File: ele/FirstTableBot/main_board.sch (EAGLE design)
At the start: 118 parts, among them IC3 CP2102N-28, T1 BC337, T2 BC337, U1 ESP-WROOM-32, X3 USB-MICRO-B-BOTTOM, X4 POWER_IN

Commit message: ir led pro encodery
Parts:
- removed !CTS, !DCD, !DSR, !DTR, !RESET, !RTS, !SUSPEND, CHR0, CHR1, CHREN, IO0/TXLED, IO1/RXLED, IO2/RS485, IO3/WAKEUP, IO4, IO5, IO6, RI/CLK, RXD, SUSPEND, TXD: PINH1X01, pinhead_smd:PINH1X01
- removed C10, C14: 100n/16V, rcl_upravena:C-EUC0402
- removed C11, C18: 4u7/16V, rcl_upravena:C-EUC0603
- removed IC3: CP2102N-28, CP2102N:CP2102N-28
- removed IM1: STEPDOWN, StepDown:STEPDOWN
- removed JP1: PINH2X06, pinhead_smd:PINH2X06
- removed LED6, LED7, LED8: yellow, led:LEDCHIP-LED0603
- removed LED_3V3: green, led:LEDCHIPLED_0603
- removed NC2: NC, NC:NC
- removed R29, R30: 180R, rcl_upravena:R-EU_R0603
- removed R31: 470R, rcl_upravena:R-EU_R0603
- removed R58: 10k, rcl_upravena:R-EU_R0603
- removed RN1: (no value), resistor-dil:2R-NEXB24V
- removed T1, T2: BC337, transistors:NPN-SOT23-BEC
- removed U1: ESP-WROOM-32, esp32:ESP-WROOM-32
- removed USB: (no value), pinhead:PINHD-1X5
- removed X3: USB-MICRO-B-BOTTOM, usb:USB-MICRO-B-BOTTOM
- added D2: (no value), diode:DIODE-D-7.5
- added IM6: DEVKITC, esp32:DEVKITC
- added JP2: (no value), pinhead:PINHD-1X6
- added R32, R33, R34, R35: (no value), resistor:R-EU_R0603
- added U$10, U$12, U$13, U$14: L-NP-3C1, led-brt:L-NP-3C1
- added U$16, U$17, U$18, U$19: BIR-NM13C1, led-brt:BIR-NM13C1
- LED0, LED1, LED2, LED3, LED4: device led:LED3MM -> led:LEDCHIPLED_1206
- LED5: value BLUE -> GREEN
- Q2, Q5: device transistors:P-MOSFET-TO220V -> transistors:P-MOSFET-MLP_HS
- R19, R62: device resistor:R-EU_M1206 -> resistor:R-EU_R0603
- R23: value 470R -> (none); device rcl_upravena:R-EU_R0603 -> resistor:R-EU_R0805
- R25, R26: value 470R -> (none); device rcl_upravena:R-EU_R0603 -> resistor:R-EU_R0603
- R27, R28: value 10k -> (none); device rcl_upravena:R-EU_R0603 -> resistor:R-EU_R0603
- RN2: device resistor-dil:4R-N0402ARV341 -> resistor-dil:4R-NEXBS8V
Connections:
- removed net !DTR: !DTR.1, IC3.!DTR, R27.1, T2.E
- removed net !DTR_B: R27.2, T1.B
- removed net !RESET: !RESET.1, IC3.!RESET, R58.1
- removed net !RTS: !RTS.1, IC3.!RTS, R28.1, T1.E
- removed net !RTS_B: R28.2, T2.B
- removed net !SUSPEND: !SUSPEND.1, IC3.!SUSPEND
- removed net CHR0: CHR0.1, IC3.CHR0
- removed net CHR1: CHR1.1, IC3.CHR1
- removed net CHREN: CHREN.1, IC3.CHREN
- removed net CLK/!RI: IC3.CLK/!RI, RI/CLK.1
- removed net DCD: !DCD.1, IC3.!DCD
- removed net DM: IC3.USBDM, USB.2, X3.D-
- removed net DP: IC3.USBDP, USB.3, X3.D+
- removed net DSR: !DSR.1, IC3.!DSR
- removed net EN: T1.C, U1.EN
- removed net IO0_!RST!_: T2.C, U1.IO0
- removed net IO12_: U1.IO12
- removed net IO13_: U1.IO13
- removed net IO14_: U1.IO14
- removed net IO15_: U1.IO15
- removed net IO16_: U1.IO16
- removed net IO17_: U1.IO17
- removed net IO18_: U1.IO18
- removed net IO19_: U1.IO19
- removed net IO21_: U1.IO21
- removed net IO22_: U1.IO22
- removed net IO23_: U1.IO23
- removed net IO25_: U1.IO25
- removed net IO26_: U1.IO26
- removed net IO27_: U1.IO27
- removed net IO2_: U1.IO2
- removed net IO32_: U1.IO32
- removed net IO33_: U1.IO33
- removed net IO34_: U1.IO34
- removed net IO35_: U1.IO35
- removed net IO4_: U1.IO4
- removed net IO5_: U1.IO5
- removed net IO9_NC1: IM1.EN, NC2.NC
- removed net LED_3V3: LED_3V3.C, R31.2
- removed net N$24: U$8.PB2/GPIO/CLK
- removed net NC-CS: U1.CMD
- removed net NC-HOLD: U1.SD2
- removed net NC-MISO: U1.SD1
- removed net NC-MOSI: U1.SD0
- removed net NC-SCK: U1.CLK
- removed net NC-WP: U1.SD3
- removed net PWM_A2: U$9.AIN2
- removed net PWM_B2: U$9.BIN2
- removed net RX-LED: LED7.C, R25.1
- removed net RXD: IC3.RXD, R30.1, RXD.1
- removed net RXD0_: R29.2, U1.RXD0
- removed net RX_LED: IC3.RXLED/IO1, IO1/RXLED.1, R25.2
- removed net SENSOR_VN_: U1.SENSOR_VN
- removed net SENSOR_VP_: U1.SENSOR_VP
- removed net SUSPEND: IC3.SUSPEND, R26.1, SUSPEND.1
- removed net TX-LED: LED6.C, R23.1
- removed net TXD: IC3.TXD, R29.1, TXD.1
- removed net TXD0_: R30.2, U1.TXD0
- removed net TX_LED: IC3.TXLED/IO0, IO0/TXLED.1, R23.2
- removed net USBID: USB.4, X3.ID
- removed net USBIO3_RS485: IC3.RS485/IO2, IO2/RS485.1
- removed net USBIO3_WAKEUP: IC3.WAKEUP/IO3, IO3/WAKEUP.1
- removed net USBIO4: IC3.IO4, IO4.1
- removed net USBIO5: IC3.IO5, IO5.1
- removed net USBIO6: IC3.IO6, IO6.1
- removed net VCCIO: C10.1, C18.1, IC3.VCC, LED6.A, LED7.A, LED8.A, R58.2
- removed net VUSB: C11.1, C14.1, IC3.VBUS, IC3.VREGIN, USB.1, X3.VBUS
- new net +5V_ESP: D2.C, IM6.5V
- new net CDA: IM6.IO2, U$8.PB2/GPIO/CLK
- new net ENC-A0: IM6.SVP, R32.2, U$10.PIN
- new net ENC-A1: IM6.SVN, R33.2, U$12.PIN
- new net ENC-B0: IM6.IO34, R34.2, U$13.PIN
- new net ENC-B1: IM6.IO35, R35.2, U$14.PIN
- new net N$18: R26.2, U$17.VCC
- new net N$19: R27.2, U$18.VCC
- new net N$20: R28.2, U$19.VCC
- new net PWM_A0: IM6.IO12, U$9.AIN1
- new net PWM_B0: IM6.IO17, U$9.BIN1
- net +3V3: now also IM6.3V3; no longer IM1.OUT, LED_3V3.A, U1.3V3
- net +5V: now also D2.A, JP2.2, R25.1, R26.1, R27.1, R28.1, R32.1, R33.1, R34.1, R35.1; no longer JP1B2.1, JP1T2.1
- net GND: now also IM6.GND, JP2.3, U$10.GND, U$12.GND, U$13.GND, U$14.GND, U$16.GND, U$17.GND, U$18.GND, U$19.GND; no longer C1.2, C10.2, C11.2, C14.2, C18.2, IC3.GND, IM1.GND, JP1B3.1, JP1T3.1, R18.2, R31.1, SW4.P, SW4.P1, U1.GND@1, U1.GND@2, U1.GND@3, U1.GND@4, USB.5, X3.GND
- net MISO: now also JP2.5; no longer JP1B5.1, JP1T5.1
- net MOSI: now also JP2.6; no longer JP1B6.1, JP1T6.1
- net N$12: now also R25.2, U$16.VCC; no longer !CTS.1, IC3.!CTS
- net N$13: now also C1.2, R18.2, SW4.P, SW4.P1; no longer LED8.C, R26.2
- net PB3: now also R23.1; no longer RN1A.1
- net PWM_A1: now also IM6.IO16, U$9.AIN2; no longer U$9.AIN1
- net PWM_B1: now also IM6.IO5, U$9.BIN2; no longer U$9.BIN1
- net RESET: now also JP2.1; no longer JP1B1.1, JP1T1.1
- net SCK: now also IM6.IO0, JP2.4; no longer JP1B4.1, JP1T4.1
- net SW4: now also R23.2; no longer RN1A.2
- net VCC: no longer IM1.IN
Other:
- note removed: "RobotikaBrno"
- note removed: "github:roboticsbrno/ RB3200-ESP32universal RobotikaBrno.cz Robotarna CC BY-SA 4.0"
- note removed: "v2.0"

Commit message: upravi elektra
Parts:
- removed JP2: (no value), pinhead:PINHD-1X6
- removed LED0: BLUE, led:LEDCHIPLED_1206
- removed RN2: (no value), resistor-dil:4R-NEXBS8V
- removed U$11: BA10358F-E2SOIC, Rohm:BA10358F-E2SOIC
- added JP1: (no value), pinhead:PINHD-1X3
- added R29, R39, R42, R45, R48: (no value), resistor:R-EU_R0805
- added R30, R31, R50, R51, R52, R53: (no value), resistor:R-EU_R0603
- added R38, R41, R44, R47: 620, resistor:R-EU_R0805
- added R40, R43, R46, R49: 10k, resistor:R-EU_R0805
- added U$15: MCP6022-E/ST, MCP6022-E_ST:MCP6022-E/ST
- LED4: value RED -> BLUE
- LED5: value GREEN -> BLUE; device led:LED3MM -> led:LEDCHIPLED_1206
- R19, R62: value (none) -> 22m
- R21, R22: value 5k -> 10k
- R23: value (none) -> 10k
- R24: value (none) -> 620; device resistor:R-EU_R0603 -> resistor:R-EU_R0805
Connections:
- removed net MISO: JP2.5, U$8.PA2/ADC/GPIO/MISO
- removed net MOSI: JP2.6, U$8.PA1/ADC/GPIO/MOSI
- removed net SW1: C3.2, JP4.8, LED2.A, RN2B.2, SW1.P, SW1.P1
- new net IR-LED-POWER: R1.1, R11.1, R13.1, R3.1, R5.1, R7.1, R9.1, U$8.PB2/CLK
- new net N$24: LED2.A, R41.2
- new net N$26: LED1.A, R38.2
- new net N$27: LED4.A, R44.2
- new net N$28: LED5.A, R47.2
- new net N$29: R51.2, R53.1, U$15.VINA-
- new net N$30: R50.2, R52.1, U$15.VINB-
- new net PC7: R47.1, R48.1, R49.1
- new net SW5: C3.2, JP4.8, R39.2, SW1.P, SW1.P1
- net +3V3: now also R30.1, R31.1
- net +5V: now also JP1.2, R23.2, R40.2, R43.2, R46.2, R49.2; no longer JP2.2, R1.1, R11.1, R13.1, R3.1, R5.1, R7.1, R9.1
- net ADC0: now also U$8.PA4/ADC; no longer U$8.PA4/ADC/GPIO
- net ADC1: now also U$8.PA5/ADC; no longer U$8.PA5/ADC/GPIO
- net ADC2: now also U$8.PA6/ADC; no longer U$8.PA6/ADC/GPIO
- net ADC3: now also U$8.PA7/ADC; no longer U$8.PA7/ADC/GPIO
- net ADC4: now also U$8.PB5/ADC; no longer U$8.PB5/ADC/GPIO
- net ADC5: now also U$8.PB4/ADC; no longer U$8.PB4/ADC/GPIO
- net ADC6: now also U$8.PB1/ADC; no longer U$8.PB1/ADC/GPIO
- net ADC7: now also U$8.PB0/ADC; no longer U$8.PB0/ADC/GPIO
- net AMPLIFIED_I-MOT_A: now also R53.2, U$15.VOUTA; no longer U$11.OUT2
- net AMPLIFIED_I-MOT_B: now also R52.2, U$15.VOUTB; no longer U$11.OUT1
- net BAT_POL+: no longer R24.2
- net CDA: now also IM6.IO22, R30.2, U$8.PA2/ADC/MISO; no longer IM6.IO2, U$8.PB2/GPIO/CLK
- net GND: now also JP1.3, R50.1, R51.1, U$15.VSS; no longer JP2.3, LED0.C, U$11.-IN1, U$11.-IN2, U$11.VEE
- net I-MOT_A: now also U$15.VINA+; no longer U$11.+IN2
- net I-MOT_B: now also U$15.VINB+; no longer U$11.+IN1
- net N$10: now also LED3.A, R24.2; no longer LED5.A, R24.1
- net PB3: now also R44.1, R45.1, R46.1, U$8.PB3/CLK; no longer R23.1, U$8.PB3/GPIO/CLK
- net PC0: now also R23.1, R24.1, R29.1, U$8.PC0/DIGITAL; no longer RN2A.1, U$8.PC0/DIGITAL/GPIO
- net PC1: now also R38.1, R39.1, R40.1, U$8.PC1/DIGITAL; no longer RN2B.1, U$8.PC1/DIGITAL/GPIO
- net PC2: now also R41.1, R42.1, R43.1, U$8.PC2/DIGITAL; no longer RN2C.1, U$8.PC2/DIGITAL/GPIO
- net PC3: now also U$8.PC3/DIGITAL; no longer RN2D.1, U$8.PC3/DIGITAL/GPIO
- net RESET: now also JP1.1, U$8.PA0/RST; no longer JP2.1, U$8.PA0/GPIO/RST
- net SCK: now also IM6.IO23, R31.2, U$8.PA3/ADC/SCK; no longer IM6.IO0, JP2.4, U$8.PA3/ADC/GPIO/SCK
- net SW0: now also R29.2; no longer LED3.A, RN2A.2
- net SW2: now also R42.2; no longer LED1.A, RN2C.2
- net SW3: now also C9.2, R45.2, R48.2, SW6.P, SW6.P1; no longer LED0.A, RN2D.2
- net SW4: no longer C9.2, LED4.A, R23.2, SW6.P, SW6.P1
- net VCC: now also U$15.VDD; no longer U$11.VCC

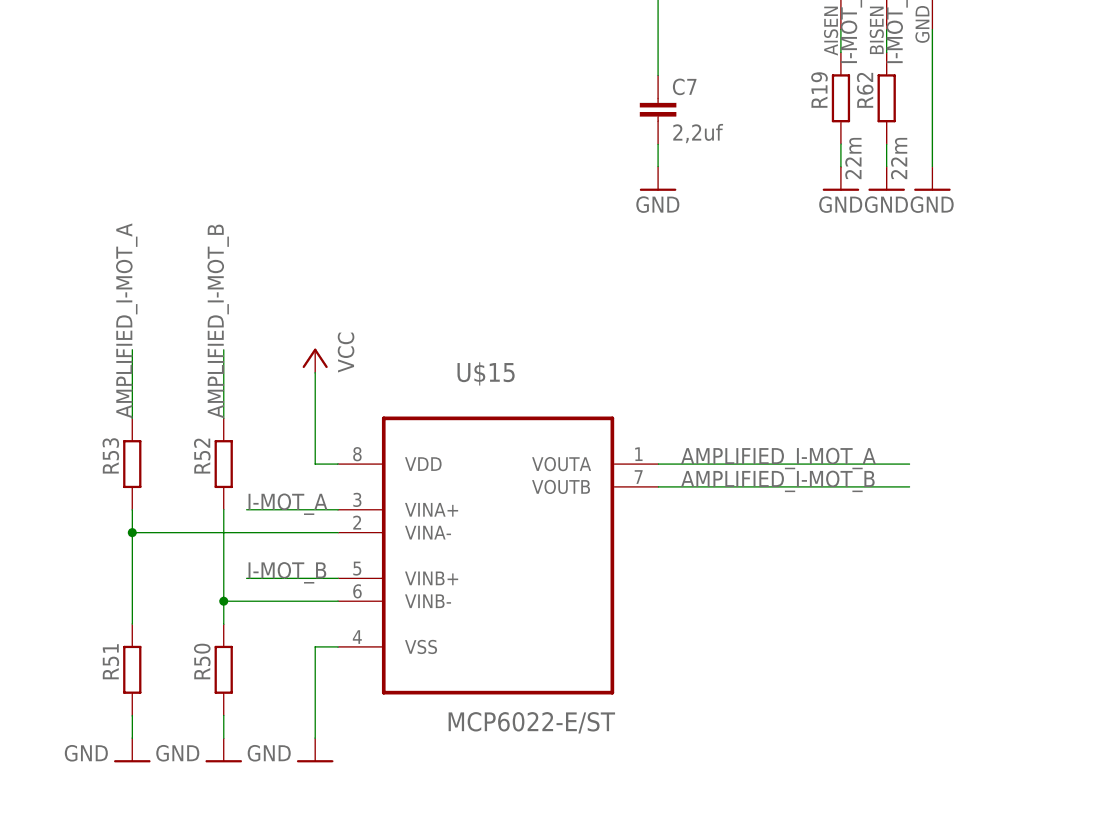
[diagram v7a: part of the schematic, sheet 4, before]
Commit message: schematická obměna OZ
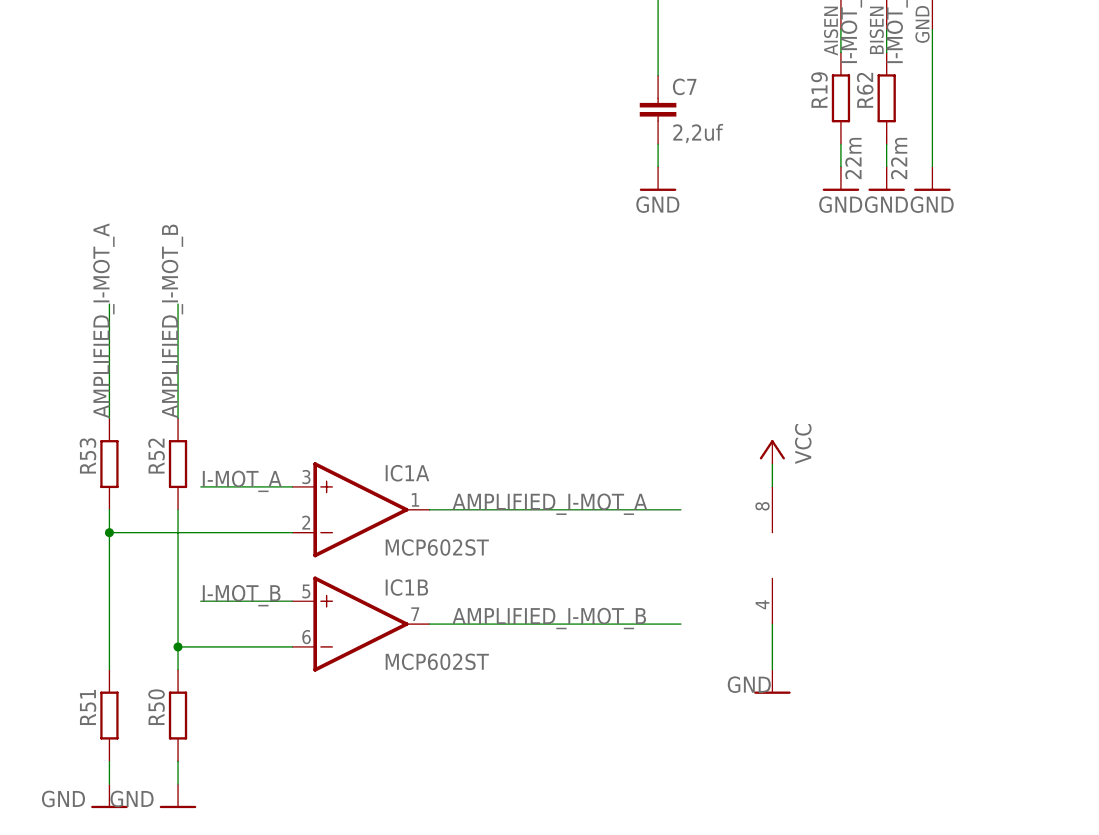
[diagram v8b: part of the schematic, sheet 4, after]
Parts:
- removed U$15: MCP6022-E/ST, MCP6022-E_ST:MCP6022-E/ST
- added IC1: MCP602ST, linear:MCP602ST
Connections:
- net RESET renamed !RESET
- net SCK renamed SCL
- net AMPLIFIED_I-MOT_A: now also IC1A.OUT; no longer U$15.VOUTA
- net AMPLIFIED_I-MOT_B: now also IC1B.OUT; no longer U$15.VOUTB
- net GND: now also IC1P.V-; no longer U$15.VSS
- net I-MOT_A: now also IC1A.+IN; no longer U$15.VINA+
- net I-MOT_B: now also IC1B.+IN; no longer U$15.VINB+
- net N$29: now also IC1A.-IN; no longer U$15.VINA-
- net N$30: now also IC1B.-IN; no longer U$15.VINB-
- net VCC: now also IC1P.V+; no longer U$15.VDD
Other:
- moved on the sheet: R50, R51, R52, R53
